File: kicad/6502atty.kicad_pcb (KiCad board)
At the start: 2 copper layers, 112.5 x 124.5 mm, 102 parts, among them J1 Conn_01x04_Pin, J10 Conn_01x04_Pin, J11 Conn_01x03_Pin, J2 Conn_01x02_Pin, J3 Conn_02x03_Odd_Even, J4 Conn_01x03_Pin, J5 Conn_01x06_Pin, J6 Conn_01x04_Pin, J7 Conn_01x10_Pin, J8 Conn_01x03_Pin, J9 Conn_01x10_Pin, SW1 SW_Push, U1 ATmega164P-20P, U10 74LS08, U11 74LS138, U12 74LS573, U2 74LS112, U3 W65C02SxP, U4 74LS573, U5 74HC245, U6 27C128, U7 KM62256CLP, U8 74LS00, U9 74LS00, Y1 18.341MHz

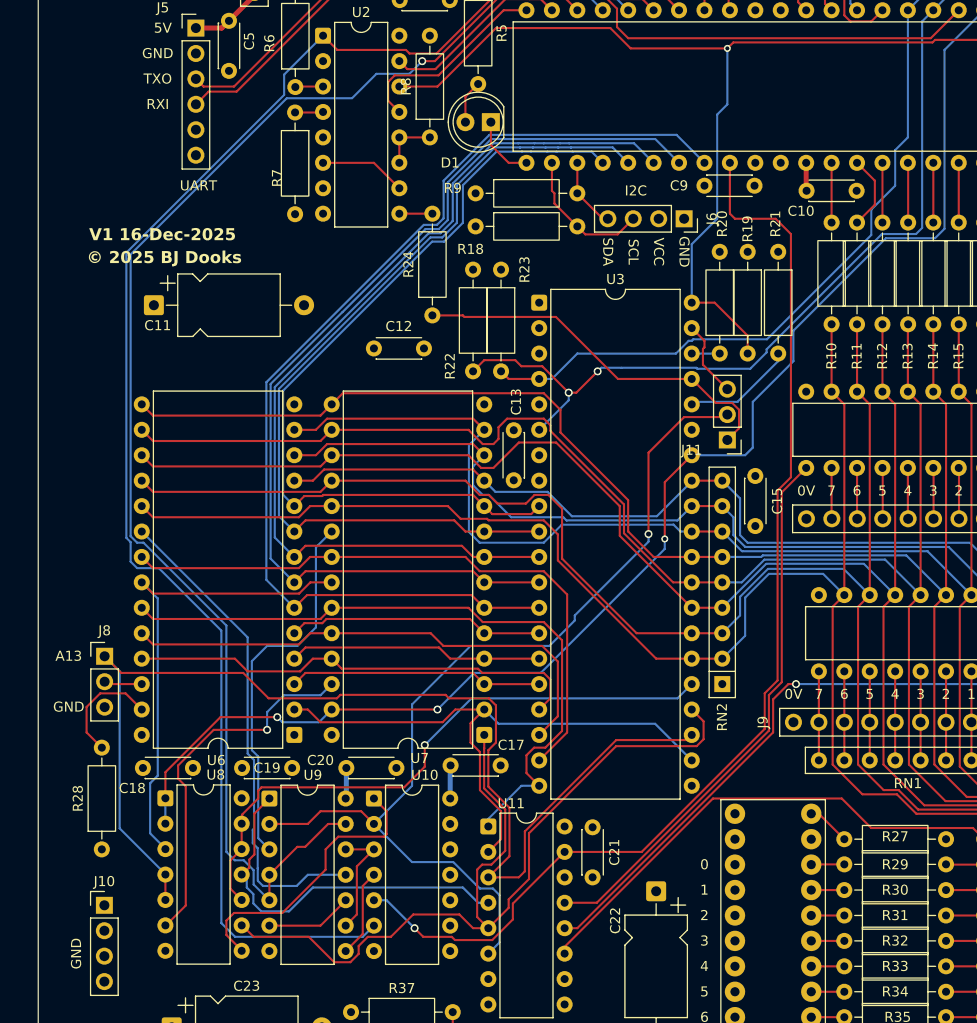
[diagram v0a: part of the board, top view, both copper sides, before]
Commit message: updates to start v1 rev2, pcb layout updates
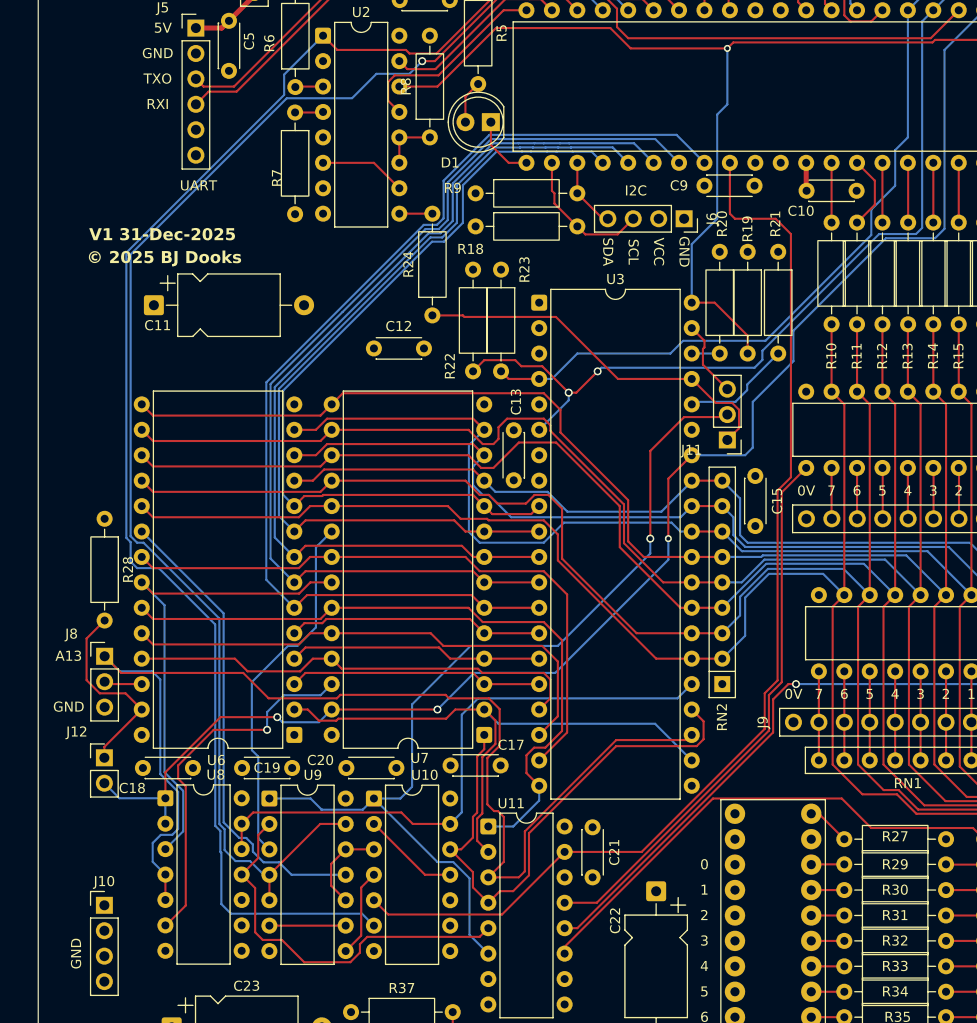
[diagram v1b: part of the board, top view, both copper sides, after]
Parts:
- added J12: Conn_01x02_Pin, Connector_PinHeader_2.54mm:PinHeader_1x02_P2.54mm_Vertical, F.Cu at (67.1, 122.9)
- moved R28 33.0 mm to (67.1, 99.1), turned to -90 degrees
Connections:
- net /~{ROM_PGM} renamed /~{ROM_PGM_WE}
- U10 pad 1: /control/ROM_AD -> /PHI2
- U10 pad 11: unconnected-(U10-Pad11) -> /control/ROM_AD
- U10 pad 12: GND -> /A14
- U10 pad 13: GND -> /A15
- U10 pad 2: /PHI2 -> /control/ROM_AD
- U11 pad 4: /control/~{A15} -> /A14
- U11 pad 5: /A14 -> /control/~{A15}
- U6 pad 1: unconnected-(U6-VPP-Pad1) -> GND
- U8 pad 10: /A15 -> GND
- U8 pad 8: /control/ROM_AD -> unconnected-(U8-Pad8)
- U8 pad 9: /A14 -> GND
- U9 pad 1: /control/~{A15} -> /PHI2
- U9 pad 10: /control/~{ROM_SEL} -> /control/ROM_ACC
- U9 pad 2: /PHI2 -> /control/~{A15}
- U9 pad 9: /control/ROM_ACC -> /control/~{ROM_SEL}
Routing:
- net /A14: track 87.5 -> 55.0 mm
- net /control/ROM_AD: track 28.5 -> 9.72 mm
- net /~{ROM_PGM_WE}: track 11.4 -> 19.8 mm
- net /R~{W}: track 138.1 -> 145.6 mm
- net VCC: track 12.6 -> 6.34 mm
- net /A13: track 116.1 -> 120.9 mm
- net /AT_~{CE}: track 112.9 -> 109.8 mm, vias 1 -> 0
- net /control/ROM_ACC: track 11.6 -> 9.12 mm
- net /control/~{A15}: track 37.6 -> 39.7 mm
- net /AT_~{EN}: track 189.3 -> 187.2 mm
- net /~{ROM_CE}: track 49.2 -> 47.2 mm
- net /ROM_SEL: track 139.4 -> 137.6 mm
- net /A15: track 61.5 -> 59.9 mm, vias 1 -> 0
- net /~{RAM_CE}: track 37.6 -> 36.3 mm
- net /control/~{ROM_SEL}: track 8.69 -> 7.62 mm
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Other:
- board text added: "V1 31-Dec-2025"
- board text removed: "V1 16-Dec-2025"

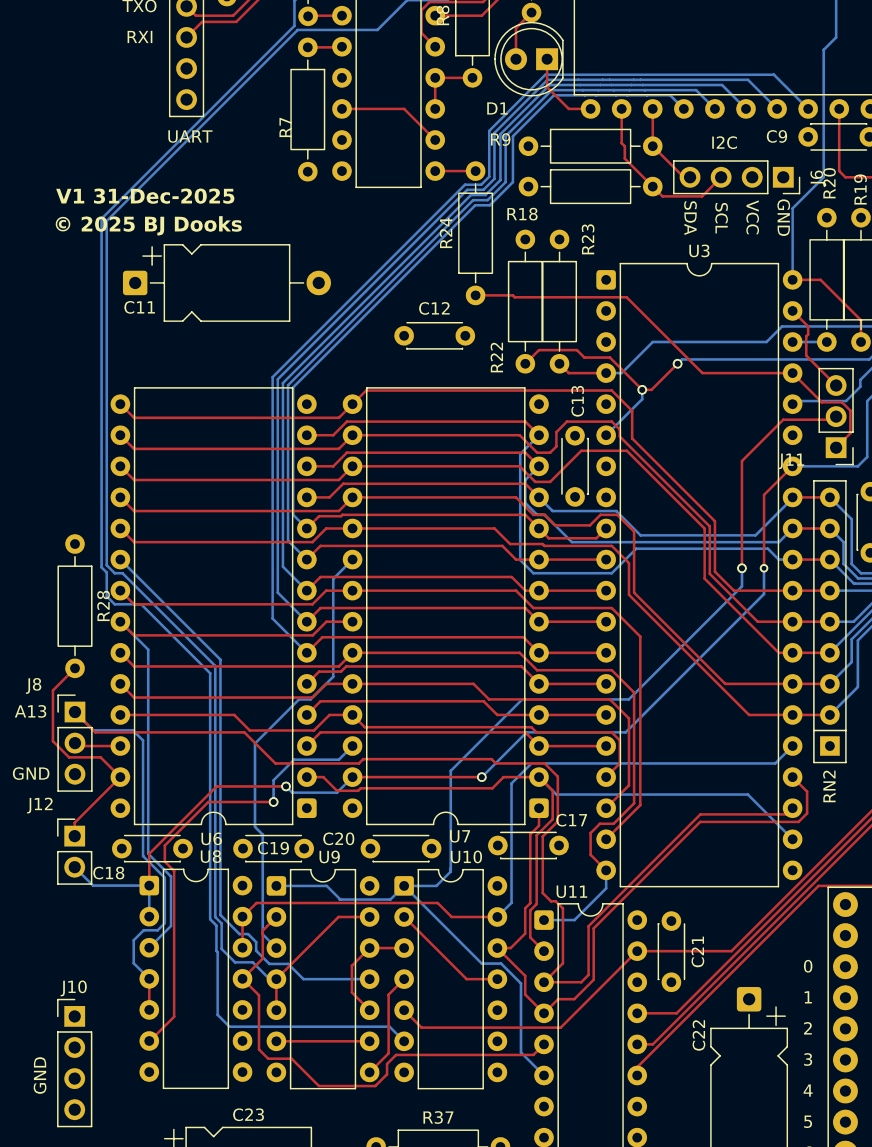
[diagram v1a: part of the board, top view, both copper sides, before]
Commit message: value updates, fix ROM ~WE
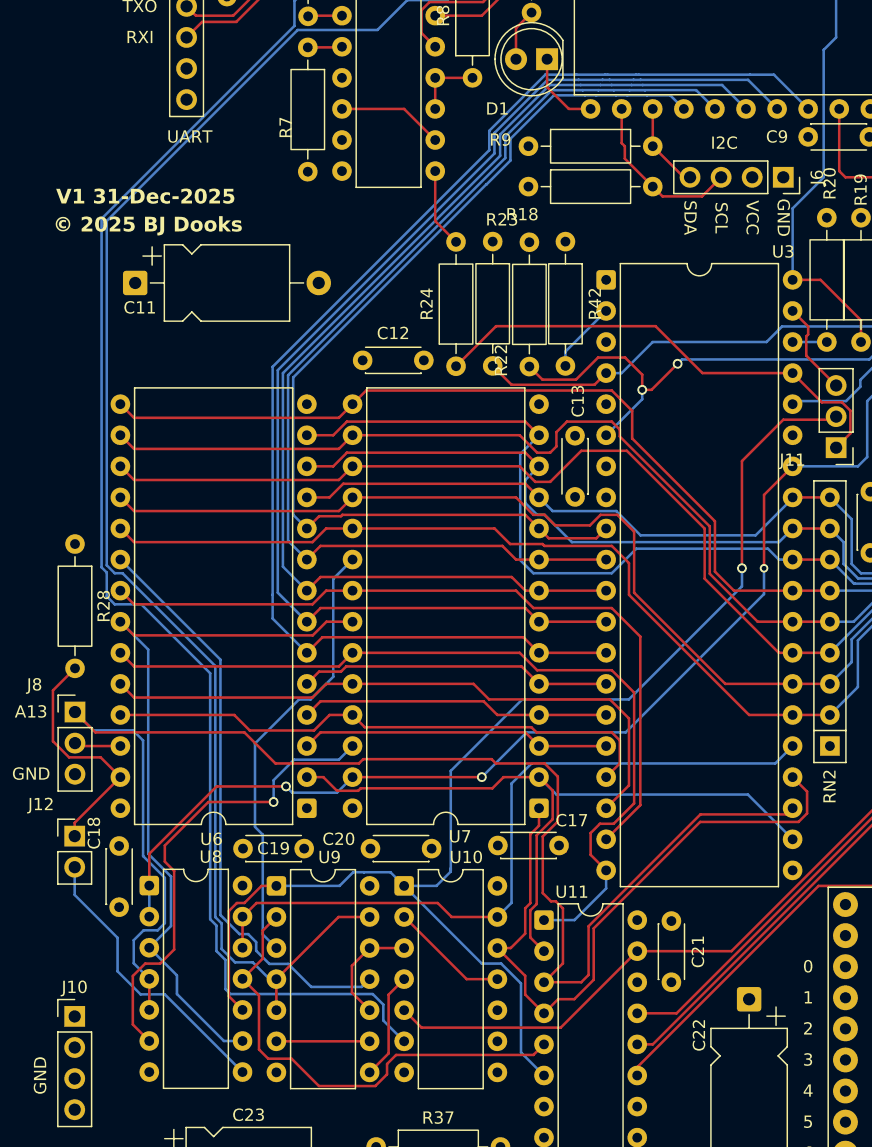
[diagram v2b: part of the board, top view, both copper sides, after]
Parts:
- added R42: R, Resistor_THT:R_Axial_DIN0207_L6.3mm_D2.5mm_P10.16mm_Horizontal, F.Cu at (107.2, 74.3)
- R19, R20, R21, R22, R23, R25, R26, R28, R36, R6, R7, R8: value R -> 4K7
- R24: value R -> 1K
- R27, R29, R30, R31, R32, R33, R34, R35, R38: value 330R -> 680R
- RN2: value R_Network08 -> 4K7
- Y1: value 18.341MHz -> 18.432MHz
- moved R24 6.00 mm to (98.2, 84.5)
- moved R23 5.46 mm to (101.2, 74.3)
- moved C12 3.94 mm to (90.6, 84.0)
- moved R22 0.40 mm to (104.2, 74.4)
- moved C18 0.31 mm to (70.7, 123.7), turned to -90 degrees
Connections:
- J12 pad 2: /R~{W} -> /R~{W}ph
- U8 pad 10: GND -> /PHI2
- U8 pad 8: unconnected-(U8-Pad8) -> /R~{W}ph
- U8 pad 9: GND -> /~{R}W
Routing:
- net /R~{W}ph: track 0.00 -> 23.6 mm
- net /PHI2: track 94.8 -> 108.0 mm
- net /~{R}W: track 49.0 -> 60.7 mm
- net /cpu/RDY: track 0.00 -> 6.95 mm
- net /R~{W}: track 145.6 -> 138.9 mm
- net /CPU_~{IRQ}: track 89.2 -> 95.4 mm
- net Net-(U2B-Q): track 3.30 -> 6.49 mm
- net /CPU_CLK: track 38.0 -> 40.0 mm
- net /~{A13}: track 36.9 -> 38.7 mm
- net /CPU_~{NMI}: track 107.0 -> 107.9 mm
- net /AT_~{EN}: track 187.2 -> 186.4 mm
- net /A4: track 106.6 -> 105.8 mm
- net /A3: track 100.3 -> 99.5 mm
- net /A1: track 88.0 -> 87.3 mm
- net /A2: track 94.1 -> 93.4 mm
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
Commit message: more updates for v1 rev2
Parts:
- removed R36: 4K7, Resistor_THT:R_Axial_DIN0207_L6.3mm_D2.5mm_P10.16mm_Horizontal
- R27, R29, R30, R31, R32, R33, R34, R35, R38: footprint Resistor_THT:R_Axial_DIN0207_L6.3mm_D2.5mm_P10.16mm_Horizontal -> Resistor_THT:R_Axial_DIN0207_L6.3mm_D2.5mm_P2.54mm_Vertical
- R39, R40: footprint Resistor_THT:R_Axial_DIN0207_L6.3mm_D2.5mm_P2.54mm_Vertical -> Resistor_THT:R_Axial_DIN0207_L6.3mm_D2.5mm_P10.16mm_Horizontal
- U12, U4: value 74LS573 -> 74LS574
- moved D2 153.5 mm to (23.9, 19.5), turned to -90 degrees
- moved R40 148.7 mm to (20.9, 52.1), turned to 0 degrees
- moved R39 148.6 mm to (20.8, 55.1), turned to 0 degrees
- moved R37 136.2 mm to (18.3, 33.6), turned to 90 degrees
- moved D3 127.5 mm to (35.9, 59.2), turned to 90 degrees
- moved D4 121.0 mm to (42.3, 59.2), turned to 90 degrees
- moved H4 63.9 mm to (113.0, 121.9)
- moved R27 63.8 mm to (95.9, 99.1)
- moved R29 63.6 mm to (95.9, 102.0)
- moved U12 63.5 mm to (107.2, 122.9)
- moved R30 63.5 mm to (95.9, 104.8)
- moved C23 63.4 mm to (112.5, 99.6), turned to -90 degrees
- moved R31 63.3 mm to (95.9, 107.7)
- moved R32 63.2 mm to (96.0, 110.4)
- moved R33 63.1 mm to (96.0, 113.2)
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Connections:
- U10 pad 1: /PHI2 -> GND
- U10 pad 10: GND -> /control/ROM_AD
- U10 pad 2: /control/ROM_AD -> GND
- U10 pad 3: /control/ROM_ACC -> unconnected-(U10-Pad3)
- U10 pad 8: unconnected-(U10-Pad8) -> /control/ROM_ACC
- U10 pad 9: GND -> /PHI2
- U12 pad 1: Net-(U12-OE) -> GND
- U7 pad 20: /~{RAM_CE} -> /A15
- U7 pad 27: /R~{W} -> /R~{W}ph
- U8 pad 1: /R~{W} -> /A13
- U8 pad 11: /control/~{A15} -> /~{R}W
- U8 pad 12: /A15 -> /R~{W}
- U8 pad 13: /A15 -> /R~{W}
- U8 pad 2: /R~{W} -> /A13
- U8 pad 3: /~{R}W -> /~{A13}
- U8 pad 4: /A13 -> GND
- U8 pad 5: /A13 -> GND
- U8 pad 6: /~{A13} -> unconnected-(U8-Pad6)
- U9 pad 1: /PHI2 -> /A15
- U9 pad 2: /control/~{A15} -> /A15
- U9 pad 3: /~{RAM_CE} -> /control/~{A15}
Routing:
- net /~{RAM_CE}: track 36.3 -> 0.00 mm
- net /A15: track 59.9 -> 95.0 mm
- net /R~{W}ph: track 23.6 -> 51.0 mm, vias 0 -> 1
- net /control/ROM_ACC: track 9.12 -> 23.9 mm
- net /D0: track 140.2 -> 127.2 mm
- net /D1: track 142.8 -> 130.1 mm
- net /A13: track 120.9 -> 109.5 mm
- net /~{A13}: track 38.7 -> 28.3 mm
- net /D2: track 150.2 -> 139.9 mm
- net Net-(D4-A): track 3.86 -> 13.2 mm
- net /CPU_~{NMI}: track 107.9 -> 99.5 mm
- net /AT_~{CE}: track 109.8 -> 118.0 mm
- net /control/ROM_AD: track 9.72 -> 2.54 mm
- net /D3: track 163.6 -> 156.5 mm
- net /D4: track 167.2 -> 160.4 mm
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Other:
- board size 112.5 x 124.5 mm -> 106.4 x 116.1 mm
- board text added: "HDR"
- board text added: "USB"
- board text removed: "5V-USB"

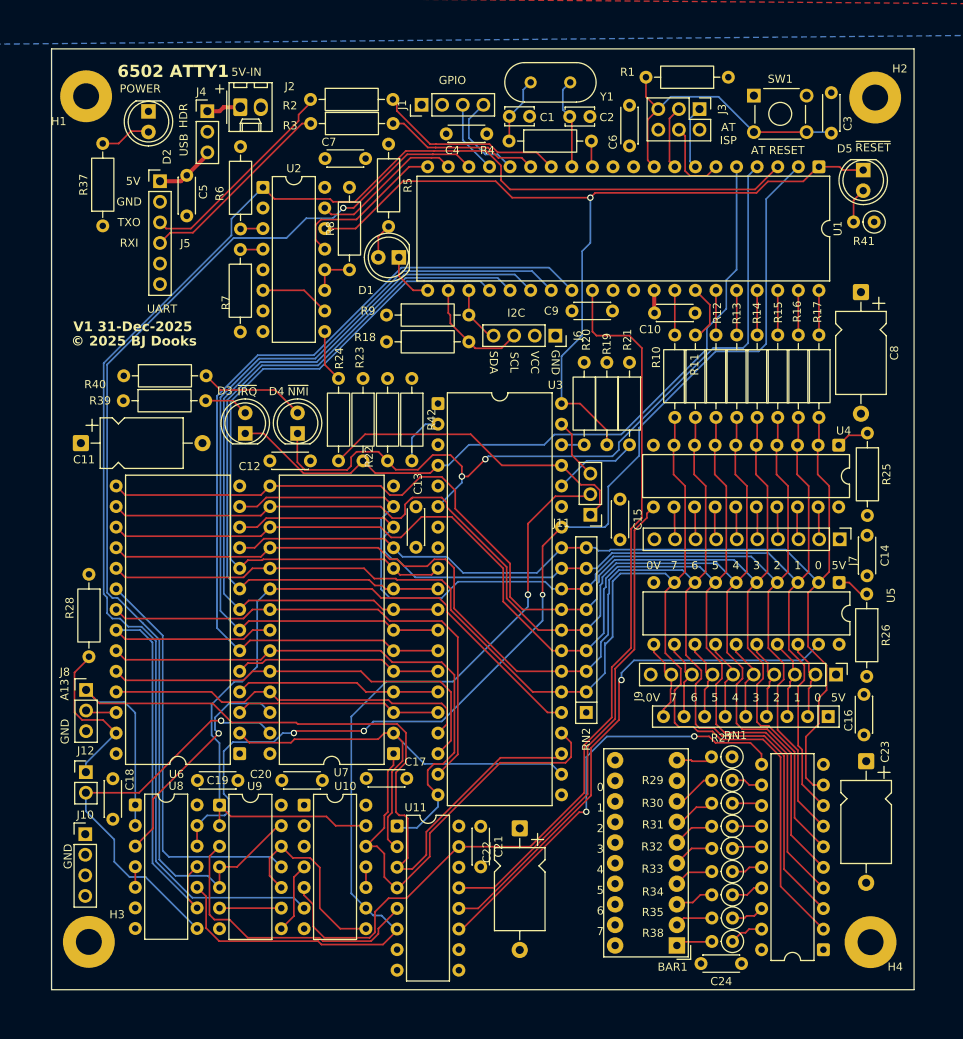
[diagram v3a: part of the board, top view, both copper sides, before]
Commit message: v1 r2: small routing and via updates
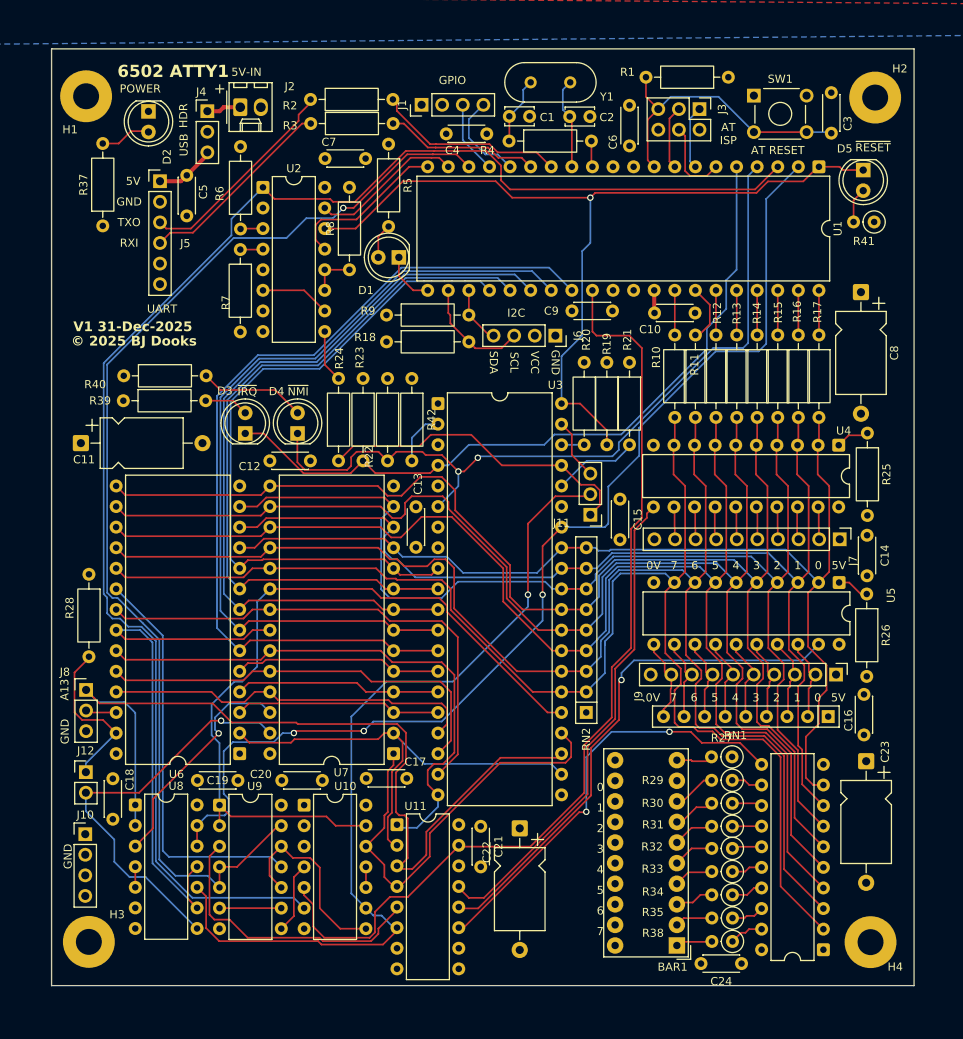
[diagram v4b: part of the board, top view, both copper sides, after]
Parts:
- moved U11 0.17 mm to (54.6, 107.5)
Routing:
- net /CPU_~{NMI}: track 99.5 -> 98.0 mm
- net /~{IO_OUT}: track 59.5 -> 60.6 mm
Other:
- board size 106.4 x 116.1 mm -> 106.4 x 115.6 mm
